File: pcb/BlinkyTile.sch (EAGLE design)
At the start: 9 parts

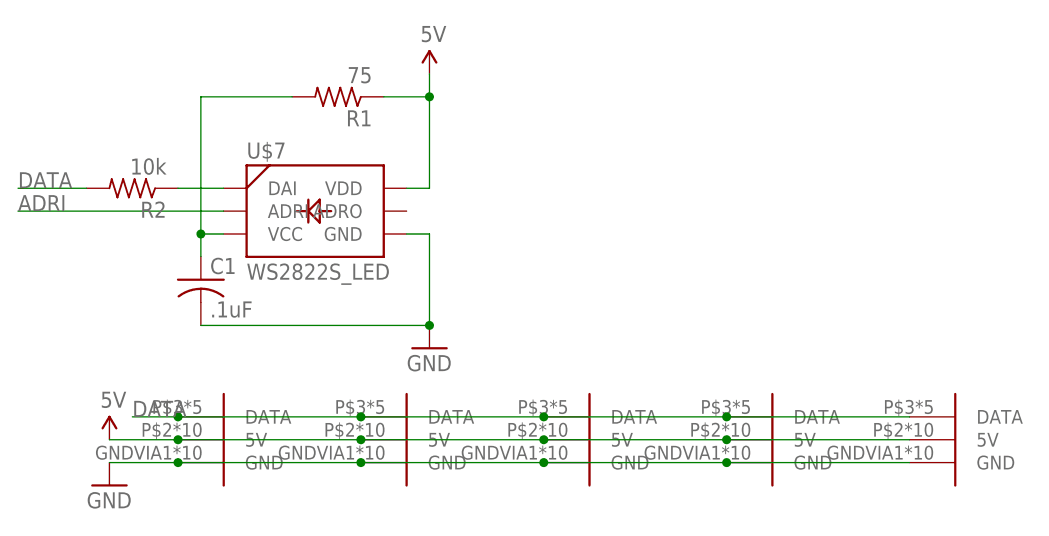
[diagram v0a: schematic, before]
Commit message: Bump to RevF: shaped solder masks for different signals
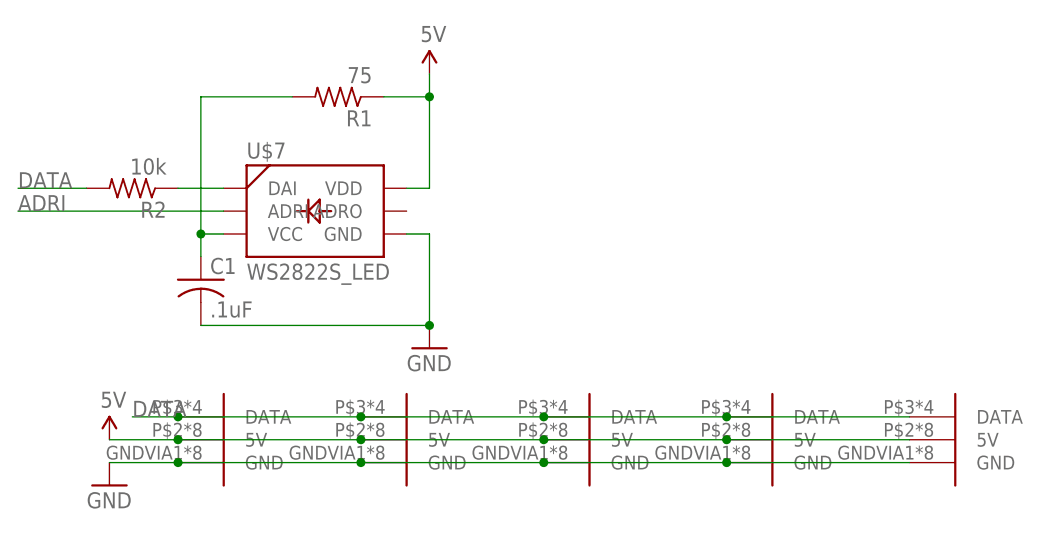
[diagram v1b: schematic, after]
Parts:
- U$2, U$3, U$4, U$5, U$6: value D_EDGESLOT -> D_EDGEMOD; device dodocohedreled:D_EDGESLOT -> dodocohedreled:D_EDGEMOD
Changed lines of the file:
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@@
 <part name="R2" library="adafruit" deviceset="R-US_" device="R0603" value="10k"/>
 <part name="SUPPLY2" library="SparkFun-Aesthetics" deviceset="5V" device=""/>
-<part name="U$2" library="dodocohedreled" deviceset="D_EDGE" device="SLOT"/>
+<part name="U$2" library="dodocohedreled" deviceset="D_EDGE" device="MOD" value="D_EDGEMOD"/>
 <part name="SUPPLY3" library="SparkFun-Aesthetics" deviceset="5V" device=""/>
 <part name="GND2" library="SparkFun-Aesthetics" deviceset="GND" device=""/>
-<part name="U$3" library="dodocohedreled" deviceset="D_EDGE" device="SLOT"/>
-<part name="U$4" library="dodocohedreled" deviceset="D_EDGE" device="SLOT"/>
-<part name="U$5" library="dodocohedreled" deviceset="D_EDGE" device="SLOT"/>
-<part name="U$6" library="dodocohedreled" deviceset="D_EDGE" device="SLOT"/>
+<part name="U$3" library="dodocohedreled" deviceset="D_EDGE" device="MOD" value="D_EDGEMOD"/>
+<part name="U$4" library="dodocohedreled" deviceset="D_EDGE" device="MOD" value="D_EDGEMOD"/>
+<part name="U$5" library="dodocohedreled" deviceset="D_EDGE" device="MOD" value="D_EDGEMOD"/>
+<part name="U$6" library="dodocohedreled" deviceset="D_EDGE" device="MOD" value="D_EDGEMOD"/>
 <part name="U$7" library="blinkinlabs" deviceset="WS2822S_LED" device=""/>
 </parts>
